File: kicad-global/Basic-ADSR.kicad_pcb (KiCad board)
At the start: 2 copper layers, 80.9 x 128.5 mm, 48 parts, among them J1 In, J2 Power Input, J3 Conn_Circuit, J4 Conn_Circuit, J5 Conn_Jack, J6 Conn_Jack, J7 Output, Q1 BC547, Q2 BC547, Q3 BC547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

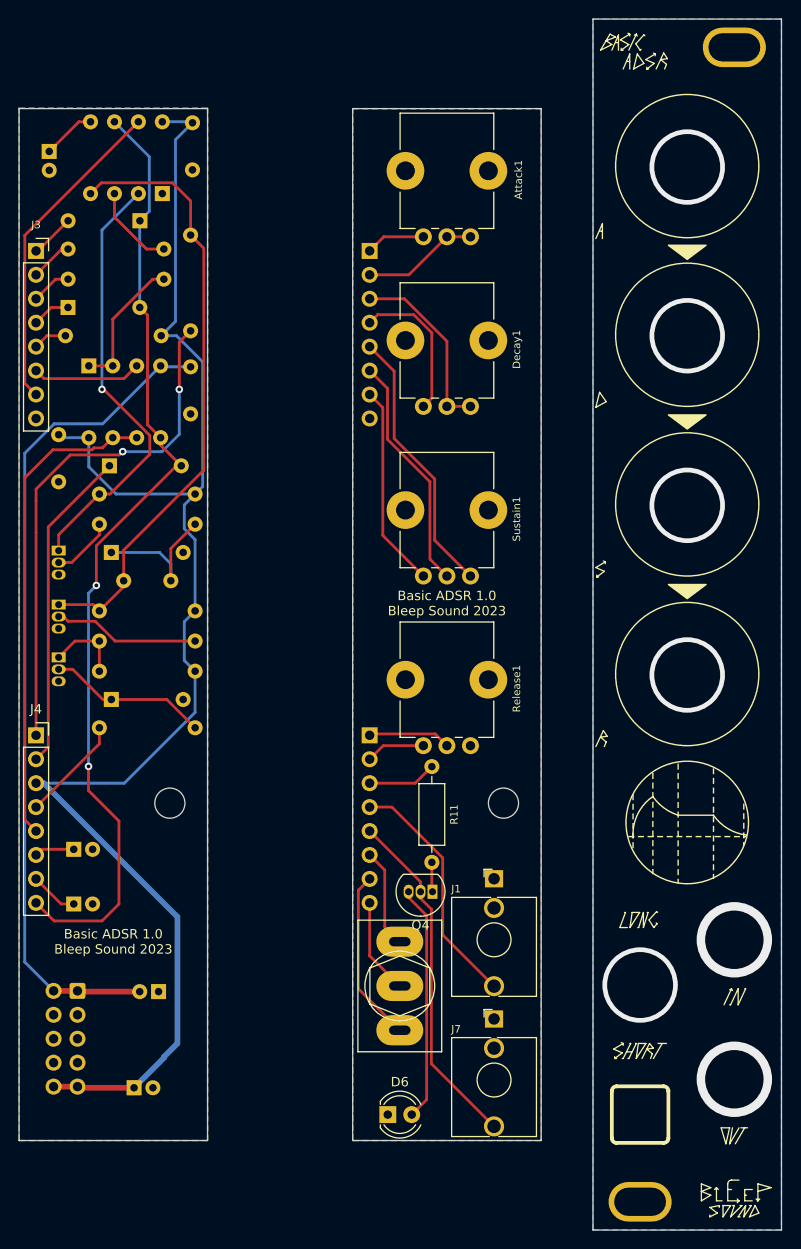
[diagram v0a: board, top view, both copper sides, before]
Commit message: update GND plane for circuitboard following issues
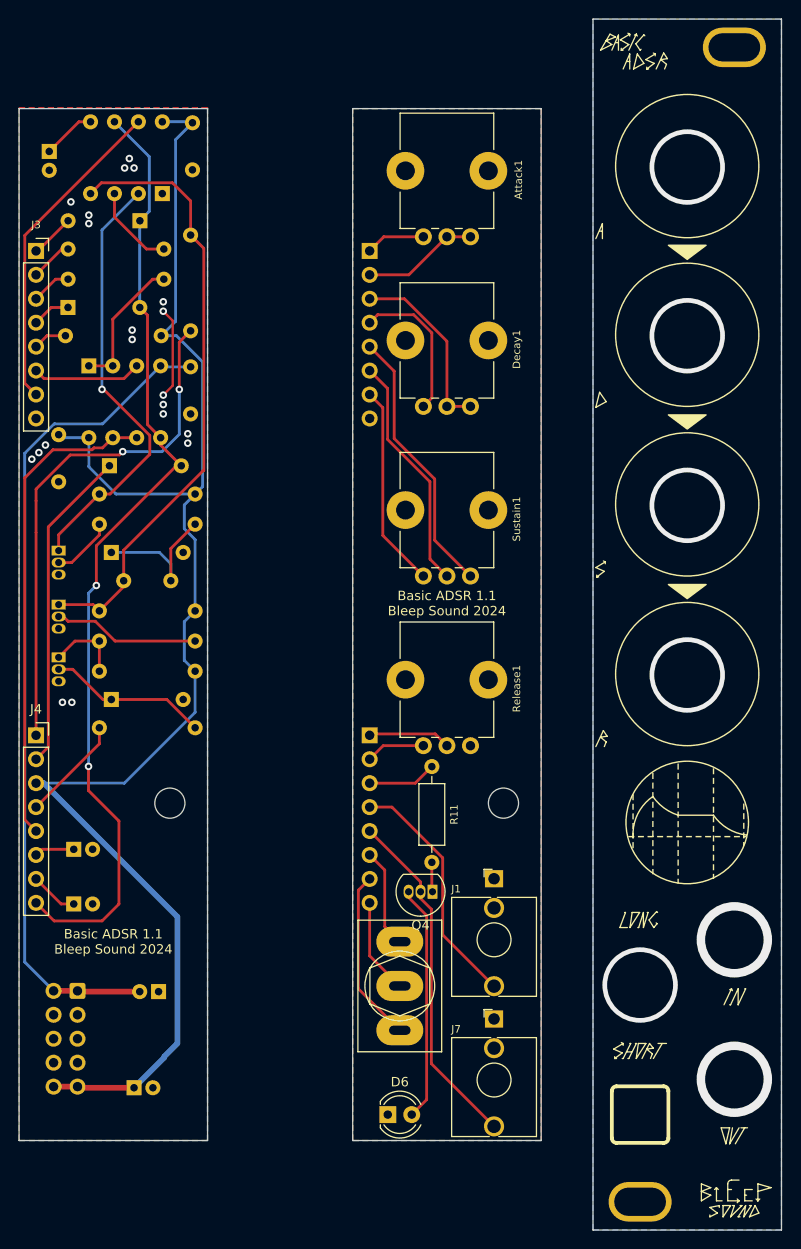
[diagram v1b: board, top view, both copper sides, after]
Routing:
- net GND: track 0.00 -> 9.73 mm, vias 7 -> 27
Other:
- board text added: "Basic ADSR 1.1 Bleep Sound 2024"
- board text removed: "Basic ADSR 1.0 Bleep Sound 2023"
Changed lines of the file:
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@@
     (effects (font (size 1 1) (thickness 0.15)) (justify mirror))
   )
-  (gr_text "Basic ADSR 1.0\nBleep Sound 2023" (at 99.5 32.5) (layer "B.SilkS")
+  (gr_text "Basic ADSR 1.1\nBleep Sound 2024" (at 99.5 32.5) (layer "B.SilkS")
     (effects (font (size 1 1) (thickness 0.15)) (justify mirror))
   )
@@
     (effects (font (size 1 1) (thickness 0.15)) (justify mirror))
   )
-  (gr_text "Basic ADSR 1.0\nBleep Sound 2023" (at 74 86.5) (layer "F.SilkS")
+  (gr_text "Basic ADSR 1.1\nBleep Sound 2024" (at 74 86.5) (layer "F.SilkS")
     (effects (font (size 1 1) (thickness 0.15)))
   )
-  (gr_text "Basic ADSR 1.0\nBleep Sound 2023" (at 38.6 122.4) (layer "F.SilkS")
+  (gr_text "Basic ADSR 1.1\nBleep Sound 2024" (at 38.6 122.4) (layer "F.SilkS")
     (effects (font (size 1 1) (thickness 0.15)))
   )
@@
     (style (thickness 0.15) (arrow_length 1.27) (text_position_mode 0) (extension_height 0.58642) (extension_offset 0.5) keep_text_aligned)
   )
+  (segment (start 43.9 64.4) (end 44.9 63.4) (width 0.25) (layer "F.Cu") (net 1))
+  (segment (start 44.9 56.5) (end 43.9 55.5) (width 0.25) (layer "F.Cu") (net 1))
+  (segment (start 44.9 63.4) (end 44.9 56.5) (width 0.25) (layer "F.Cu") (net 1))
   (via (at 94.5 127) (size 8) (drill 7) (layers "F.Cu" "B.Cu") (free) (net 1))
+  (via (at 29.9495 71.2) (size 0.8) (drill 0.4) (layers "F.Cu" "B.Cu") (free) (net 1))
+  (via (at 36 45.3) (size 0.8) (drill 0.4) (layers "F.Cu" "B.Cu") (free) (net 1))
+  (via (at 43.9 64.4) (size 0.8) (drill 0.4) (layers "F.Cu" "B.Cu") (free) (net 1))
+  (via (at 46.5 68.5) (size 0.8) (drill 0.4) (layers "F.Cu" "B.Cu") (free) (net 1))
+  (via (at 40.8 40.3) (size 0.8) (drill 0.4) (layers "F.Cu" "B.Cu") (free) (net 1))
   (via (at 104.5 122.2) (size 8) (drill 6.2) (layers "F.Cu" "B.Cu") (free) (net 1))
+  (via (at 30.7 70.5) (size 0.8) (drill 0.4) (layers "F.Cu" "B.Cu") (free) (net 1))
+  (via (at 43.9 55.5) (size 0.8) (drill 0.4) (layers "F.Cu" "B.Cu") (free) (net 1))
   (via (at 99.5 76.1) (size 8) (drill 7) (layers "F.Cu" "B.Cu") (free) (net 1))
+  (via (at 33.2 97) (size 0.8) (drill 0.4) (layers "F.Cu" "B.Cu") (free) (net 1))
+  (via (at 31.4 69.7) (size 0.8) (drill 0.4) (layers "F.Cu" "B.Cu") (free) (net 1))
+  (via (at 40.6 57.5) (size 0.8) (drill 0.4) (layers "F.Cu" "B.Cu") (free) (net 1))
+  (via (at 43.9 66.4) (size 0.8) (drill 0.4) (layers "F.Cu" "B.Cu") (free) (net 1))
+  (via (at 34.1 43.9) (size 0.8) (drill 0.4) (layers "F.Cu" "B.Cu") (free) (net 1))
+  (via (at 34.2 97) (size 0.8) (drill 0.4) (layers "F.Cu" "B.Cu") (free) (net 1))
+  (via (at 43.9 65.4) (size 0.8) (drill 0.4) (layers "F.Cu" "B.Cu") (free) (net 1))
   (via (at 99.5 94.1) (size 8) (drill 7) (layers "F.Cu" "B.Cu") (free) (net 1))
+  (via (at 46.5 69.5) (size 0.8) (drill 0.4) (layers "F.Cu" "B.Cu") (free) (net 1))
+  (via (at 39.8 40.3) (size 0.8) (drill 0.4) (layers "F.Cu" "B.Cu") (free) (net 1))
   (via (at 99.5 58.1) (size 8) (drill 7) (layers "F.Cu" "B.Cu") (free) (net 1))
+  (via (at 40.6 58.5) (size 0.8) (drill 0.4) (layers "F.Cu" "B.Cu") (free) (net 1))
+  (via (at 36 46.2) (size 0.8) (drill 0.4) (layers "F.Cu" "B.Cu") (free) (net 1))
+  (via (at 40.3 39.3) (size 0.8) (drill 0.4) (layers "F.Cu" "B.Cu") (free) (net 1))
+  (via (at 43.9 54.5) (size 0.8) (drill 0.4) (layers "F.Cu" "B.Cu") (free) (net 1))
   (via (at 99.5 40.2) (size 8) (drill 7) (layers "F.Cu" "B.Cu") (free) (net 1))
   (via (at 104.5 137) (size 8) (drill 6.2) (layers "F.Cu" "B.Cu") (free) (net 1))
